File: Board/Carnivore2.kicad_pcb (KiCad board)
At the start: 2 copper layers, 99.1 x 64.3 mm, 153 parts, among them J1 Conn_01x02_Pin, T1 2SC945, T2 2SA733, T3 2SC945, T4 2SC945, T5 2SC945, T6 2SA733, U7 50 MHz, U8 DNI, X1 EDGE50/MSX, X2 HEADER_5X2, X3 HEADER_5X2

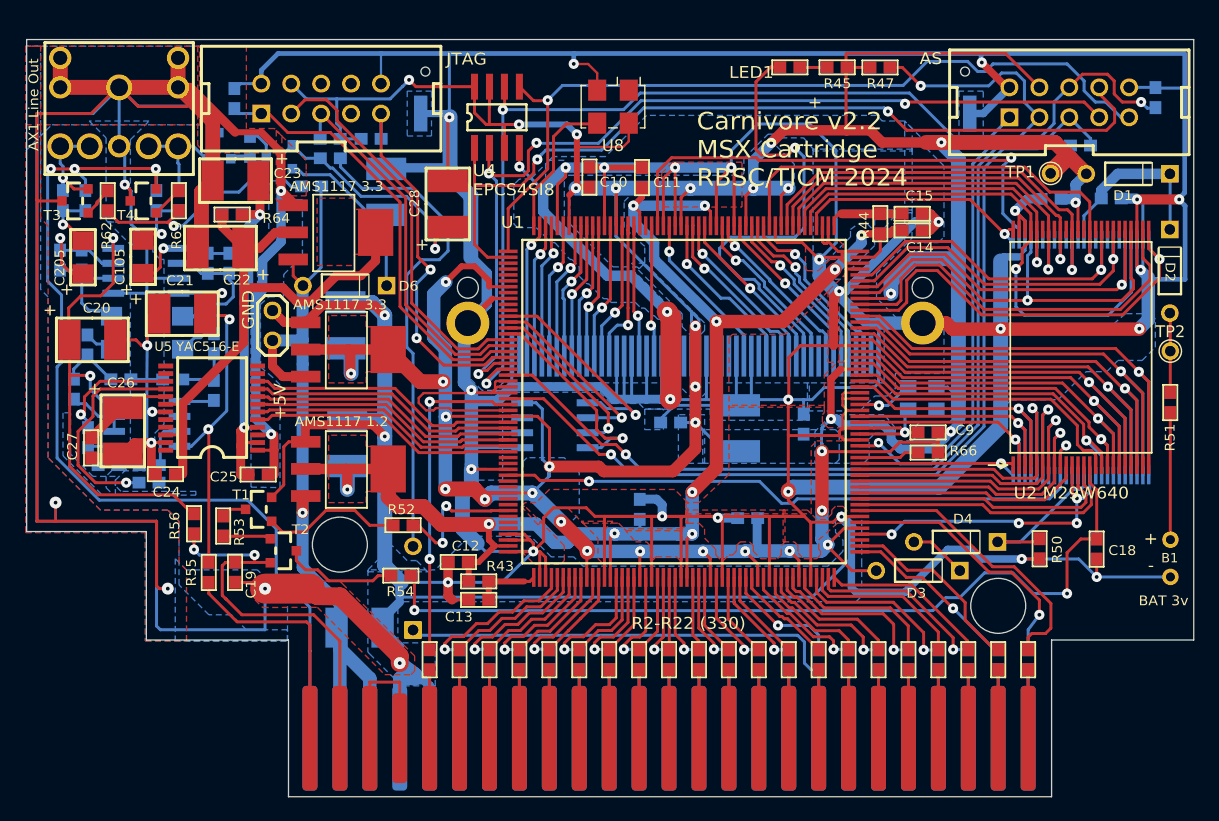
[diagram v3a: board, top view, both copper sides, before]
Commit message: Changed fpga from EP2C5 to EP2C8
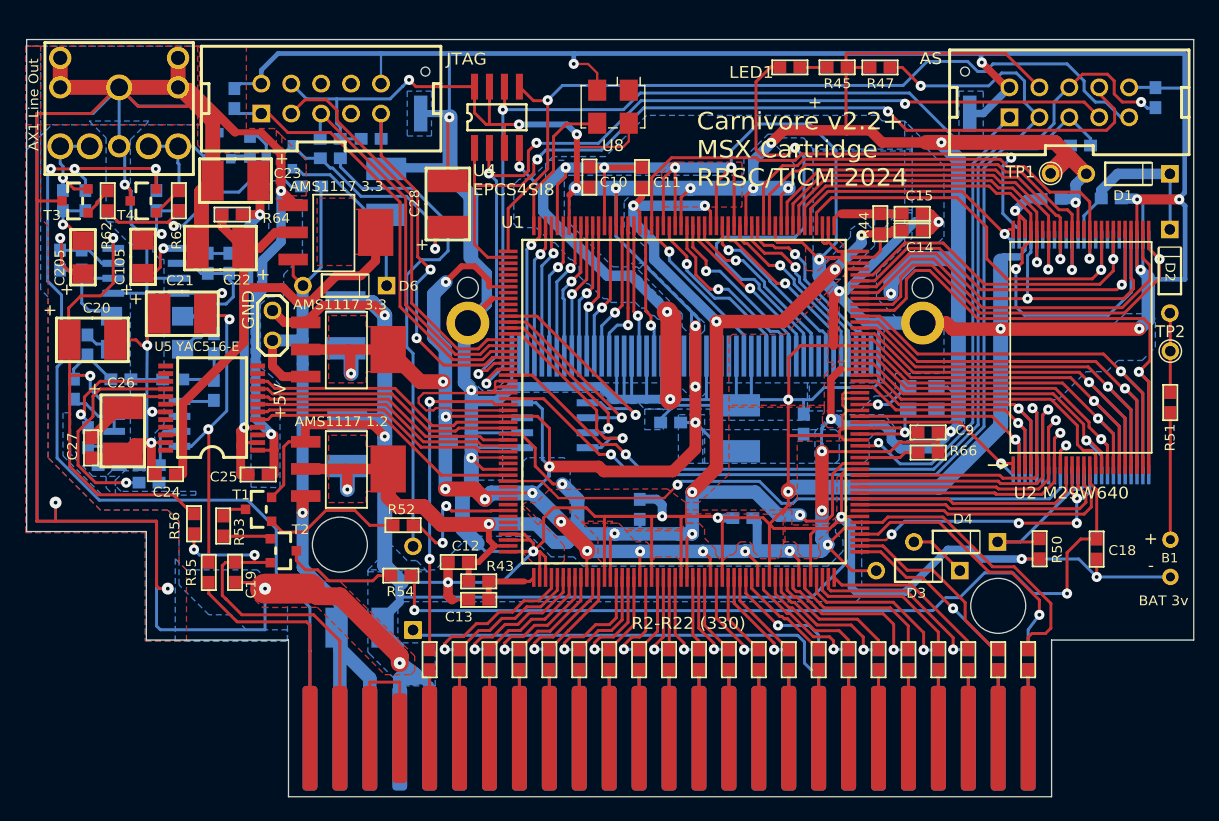
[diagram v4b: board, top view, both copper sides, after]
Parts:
- moved C8 0.41 mm to (155.4, 111.5)
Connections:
- U1 pad 107: unconnected-(U1B-IO,_LVDS41n_(INIT_DONE)-Pad107) -> /~{RWR}
- U1 pad 108: /~{RWR} -> /~{SLT_CS1}
- U1 pad 110: /~{SLT_CS1} -> /~{SLT_CS2}
- U1 pad 112: /~{SLT_CS2} -> /RA21
- U1 pad 113: /RA21 -> /~{RRP}
- U1 pad 114: /~{RRP} -> /RA20
- U1 pad 115: /RA20 -> /RA08
- U1 pad 116: /RA08 -> /RA09
- U1 pad 117: /RA09 -> /RA10
- U1 pad 118: /RA10 -> /RA11
- U1 pad 119: /RA11 -> /GND
- U1 pad 120: /RA15 -> /VCC1.2
- U1 pad 127: /RA14 -> /RA15
- U1 pad 128: /RA13 -> /RA14
- U1 pad 133: /RA12 -> /RA13
- U1 pad 134: /~{RRB} -> /RA12
- U1 pad 135: /RA18 -> /~{RRB}
- U1 pad 137: /RA17 -> /RA18
- U1 pad 138: /RA07 -> /RA17
- U1 pad 139: /RA06 -> /RA07
- U1 pad 141: /RA05 -> /RA06
- U1 pad 142: /RA04 -> /RA05
- U1 pad 143: /RA03 -> /RA04
- U1 pad 144: /RA02 -> /RA03
- U1 pad 145: /RA01 -> /RA02
- U1 pad 146: /RA00 -> /RA01
- U1 pad 147: /R~{E} -> /RA00
- U1 pad 149: /R~{G} -> /R~{E}
- U1 pad 150: /RDQ0 -> /R~{G}
- U1 pad 151: /RDQ1 -> /RDQ0
- U1 pad 152: /RDQ2 -> /RDQ1
- U1 pad 160: /RA16 -> /RDQ2
- U1 pad 161: /RDQ15A-1 -> /RA16
- U1 pad 162: /RDQ7 -> /RDQ15A-1
- U1 pad 163: /RDQ6 -> /RDQ7
- U1 pad 164: /RDQ5 -> /RDQ6
- U1 pad 165: /RDQ4 -> /RDQ5
- U1 pad 168: /RDQ3 -> /RDQ4
- U1 pad 169: /HD10 -> /RDQ3
- U1 pad 170: /HD09 -> /HD10
- U1 pad 171: /HD02 -> /HD09
- U1 pad 173: /HD08 -> /HD02
- U1 pad 175: /HD01 -> /HD08
- U1 pad 176: /HD00 -> /HD01
- U1 pad 179: /HA0 -> /HD00
- U1 pad 180: /~{HREG} -> /HA0
- U1 pad 181: /HA1 -> /~{HREG}
- U1 pad 182: /HA2 -> /HA1
- U1 pad 185: /~{HRST} -> /HA2
- U1 pad 187: /~{CSRAM} -> /~{HRST}
- U1 pad 188: /~{HWR} -> /~{CSRAM}
- U1 pad 189: unconnected-(U1A-IO,_LVDS19n,_DQ1T2/DQ1T11-Pad189) -> /~{HWR}
- U1 pad 32: /BICK -> /VCC1.2
- U1 pad 33: /CKS -> /BICK
- U1 pad 34: /MCLK -> /CKS
- U1 pad 35: /~{IC} -> /MCLK
- U1 pad 36: unconnected-(U1A-IO,_LVDS2n-Pad36) -> /GND
- U1 pad 39: /RA19 -> /~{IC}
- U1 pad 40: unconnected-(U1A-IO,_LVDS1p,_DQ1L8/_-Pad40) -> /RA19
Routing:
- net /VCC1.2: track 123.9 -> 155.3 mm, vias 10 -> 12
- net /RA01: track 43.1 -> 50.7 mm
- net /RDQ2: track 29.3 -> 36.5 mm
- net /GND: track 1229.9 -> 1233.3 mm
- net /RDQ4: track 35.9 -> 38.4 mm
- net /HD02: track 14.4 -> 16.0 mm
- net /RA15: track 14.5 -> 16.0 mm
- net /RA16: track 20.6 -> 21.9 mm
- net /RDQ15A-1: track 45.0 -> 46.2 mm
- net /RDQ7: track 28.9 -> 30.1 mm
- net /RDQ6: track 31.8 -> 33.1 mm
- net /RDQ5: track 31.9 -> 33.2 mm
- net /R~{E}: track 34.2 -> 33.0 mm
- net /HD00: track 14.5 -> 15.6 mm
- net /RA13: track 22.2 -> 23.2 mm
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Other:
- board text added: "Carnivore v2.2+ MSX Cartridge RBSC/TICM 2024"
- board text removed: "Carnivore v2.2 MSX Cartridge RBSC/TICM 2024"

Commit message: Changed audio DAC to modern type, added audio input, updated footprints
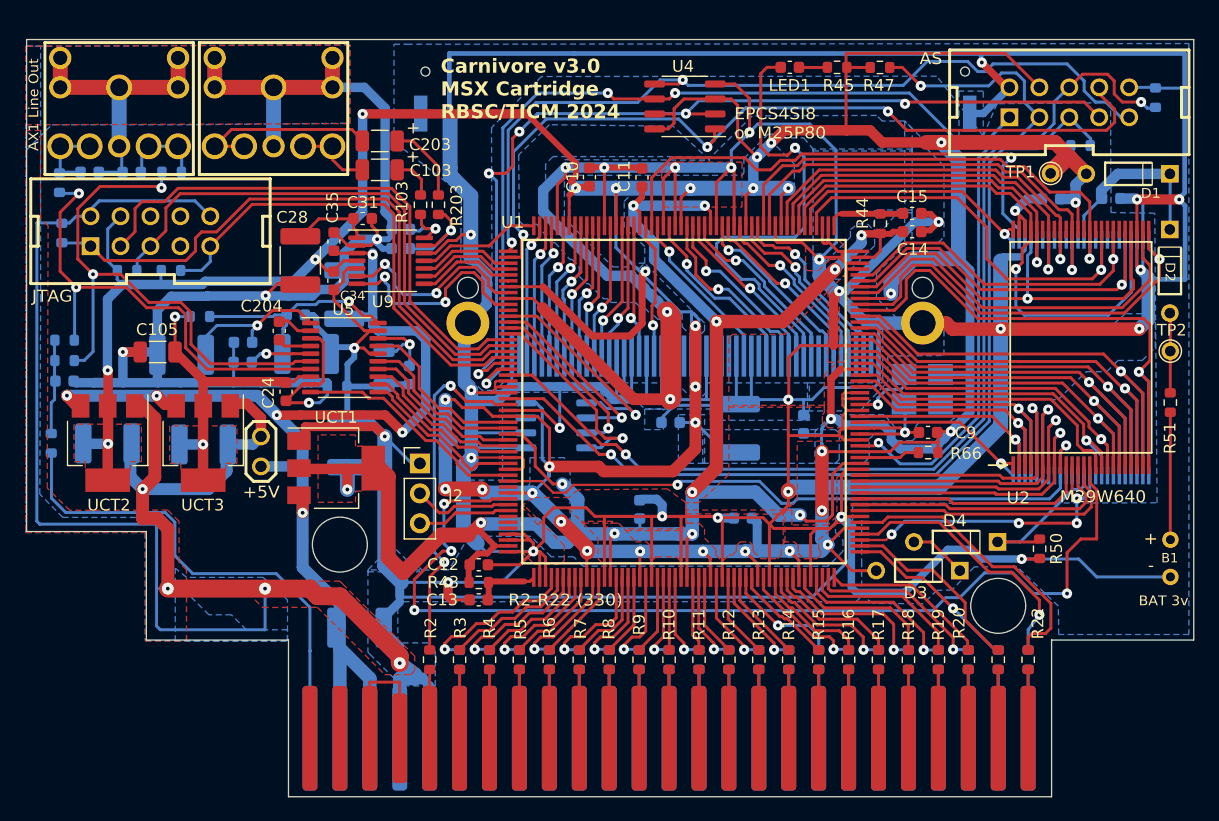
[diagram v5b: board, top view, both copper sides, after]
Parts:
- removed AU1, AU2: ~, Library:4558D_1
- removed C18, C19: 0.1mk, Library:C_0603_1
- removed C20, C21: 100mk 16v, Library:C_1812_1
- removed C202: 1n, Library:C_0603_1
- removed D5, D6: 1N4148, Library:DIODE_1N4148_1
- removed R101, R201, R52, R65: 10k, Library:R_0603_1
- removed R102, R202: 4.7k, Library:R_0603_1
- removed R105, R205: 1.8k, Library:R_0603_1
- removed R106, R206: 1k, Library:R_0603_1
- removed R53, R62, R63: 2.2k, Library:R_0603_1
- removed R54: 10, Library:R_0603_1
- removed R55, R56: 220, Library:R_0603_1
- removed T1, T3, T4, T5: 2SC945, Library:SOT-23(A1A2K)_1
- removed T2, T6: 2SA733, Library:SOT-23(A1A2K)_1
- removed U8: DNI, Oscillator:Oscillator_SMD_TXC_7C-4Pin_5.0x3.2mm_HandSoldering
- added AX2: {Value}, Library:ST-222_1, F.Cu at (115.5, 74.9)
- added C31: 100nF, Capacitor_SMD:C_0603_1608Metric, F.Cu at (123.1, 86.0)
- added C32: 100nF, Capacitor_SMD:C_0603_1608Metric, B.Cu at (126.3, 86.9)
- added C33: 100nF, Capacitor_SMD:C_0603_1608Metric, B.Cu at (126.3, 88.6)
- added C34: 100nF, Capacitor_SMD:C_0603_1608Metric, F.Cu at (120.7, 91.3)
- added C35: 100nF, Capacitor_SMD:C_0603_1608Metric, F.Cu at (120.7, 88.0)
- added C36: 2.2nF, Capacitor_SMD:C_0603_1608Metric, B.Cu at (97.8, 99.8)
- added J2: Conn_01x03_Pin, Connector_PinHeader_2.54mm:PinHeader_1x03_P2.54mm_Vertical, F.Cu at (128.0, 106.8)
- added R49: 470, Resistor_SMD:R_0603_1608Metric, B.Cu at (97.8, 98.1)
- added R99: 10, Resistor_SMD:R_0603_1608Metric, B.Cu at (120.9, 100.3)
- added U9: ~, Package_SO:TSSOP-14_4.4x5mm_P0.65mm, F.Cu at (125.5, 89.6)
- C1, C2, C3, C4: footprint Library:C_1812_1 -> Capacitor_SMD:C_1812_4532Metric
- C10, C11, C12, C13, C14, C15, C16, C17, C30, C5, C6, C7, C8, C9, LED1: footprint Library:C_0603_1 -> Capacitor_SMD:C_0603_1608Metric
- C101, C201: value 1n -> 2.2nF; footprint Library:C_0603_1 -> Capacitor_SMD:C_0603_1608Metric
- C102: value 1n -> 100nF; footprint Library:C_0603_1 -> Capacitor_SMD:C_0603_1608Metric
- C103, C203: value 4.7mk 25v -> 10uF 16V; footprint Library:C_1206_1 -> Capacitor_SMD:C_1206_3216Metric; moved to F.Cu
- C104: value 390p -> 2.2uF; footprint Library:C_0603_1 -> Capacitor_SMD:C_0603_1608Metric
- C105: value 4.7mk 25v -> 10uF 16V; footprint Library:C_1206_1 -> Capacitor_SMD:C_1206_3216Metric
- C204: value 390p -> 2.2uF; footprint Library:C_0603_1 -> Capacitor_SMD:C_0603_1608Metric; moved to F.Cu
- C205: value 4.7mk 25v -> 10uF 16V; footprint Library:C_1206_1 -> Capacitor_SMD:C_1206_3216Metric; moved to B.Cu
- C22: footprint Library:C_1812_1 -> Capacitor_SMD:C_1812_4532Metric; moved to B.Cu
- C23, C26: value 10mk -> 10uF 16V; footprint Library:C_1812_1 -> Capacitor_SMD:C_1812_4532Metric; moved to B.Cu
- C24: value 0.1mk -> 100nF; footprint Library:C_0603_1 -> Capacitor_SMD:C_0603_1608Metric
- C25, C27: value 0.1mk -> 100nF; footprint Library:C_0603_1 -> Capacitor_SMD:C_0603_1608Metric; moved to B.Cu
- C28: value 10mk -> 10uF 16v; footprint Library:C_1812_1 -> Capacitor_SMD:C_1812_4532Metric
- C29: value 22mk -> 10uF 16V; footprint Library:C_1812_1 -> Capacitor_SMD:C_1812_4532Metric
- R10, R11, R12, R13, R14, R15, R16, R17, R18, R19, R2, R20, R21, R22, R23, R24, R25, R26, R27, R28, R29, R3, R30, R31, R32, R33, R34, R35, R36, R37, R38, R39, R4, R40, R41, R42, R43, R44, R45, R46, R47, R48, R5, R50, R51, R57, R58, R59, R6, R66, R7, R8, R9: footprint Library:R_0603_1 -> Resistor_SMD:R_0603_1608Metric
- R103, R203: footprint Library:R_0603_1 -> Resistor_SMD:R_0603_1608Metric; moved to F.Cu
- R104, R204: value 100k -> 470; footprint Library:R_0603_1 -> Resistor_SMD:R_0603_1608Metric
- R60: value 10k -> 470; footprint Library:R_0603_1 -> Resistor_SMD:R_0603_1608Metric
- R61: value 2.2k -> 470; footprint Library:R_0603_1 -> Resistor_SMD:R_0603_1608Metric
- R64: footprint Library:R_0603_1 -> Resistor_SMD:R_0603_1608Metric; moved to B.Cu
- U4: footprint Library:EPCS4SI8_1 -> Package_SO:SO-8_3.9x4.9mm_P1.27mm
- U5: footprint Library:YAC516-E_1 -> Package_SO:TSSOP-20_4.4x6.5mm_P0.65mm
- U6: footprint Library:M93C46MN1_1 -> Package_SO:SO-8_3.9x4.9mm_P1.27mm
- U7: footprint Library:SG-310_1 -> Oscillator:Oscillator_SMD_SeikoEpson_SG8002CE-4Pin_3.2x2.5mm_HandSoldering
- UCT1, UCT2, UCT3: footprint Library:ADP3338_1 -> Package_TO_SOT_SMD:SOT-223
- moved R203 32.1 mm to (129.5, 84.8), turned to 90 degrees
- moved R61 30.3 mm to (96.7, 105.1), turned to -90 degrees
- moved C203 28.0 mm to (124.5, 79.4), turned to 180 degrees
- moved R60 27.3 mm to (97.8, 96.3)
- moved C205 27.2 mm to (124.9, 98.7)
- moved C201 24.9 mm to (99.9, 82.1), turned to 0 degrees
- moved C101 24.9 mm to (103.5, 82.1)
- moved C2 22.5 mm to (101.4, 105.1), turned to 180 degrees
- moved C103 21.7 mm to (124.5, 81.9), turned to 180 degrees
- moved UCT3 21.6 mm to (109.6, 105.1)
- moved R103 21.1 mm to (128.0, 84.8), turned to 90 degrees
- moved R58 20.5 mm to (103.1, 90.4)
- moved R59 20.3 mm to (106.8, 90.4), turned to 0 degrees
- moved C102 20.1 mm to (127.0, 99.3), turned to 90 degrees
- moved UCT2 19.7 mm to (101.5, 105.1)
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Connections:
- net /CONF_DONE renamed Net-(U1C-CONF_DONE)
- net /~{SLT_RESET_RAW} renamed Net-(R30-Pad2)
- AX1 pad 1: /GND -> /AGND
- AX1 pad 2: Net-(T5-E) -> Net-(AX1-Pad2)
- AX1 pad 3: Net-(T5-E) -> Net-(AX1-Pad2)
- AX1 pad 4: Net-(T3-E) -> Net-(AX1-Pad4)
- AX1 pad 5: Net-(T3-E) -> Net-(AX1-Pad4)
- AX1 pad M: /GND -> /AGND
- C101 pad 1: /GND -> /AGND
- C101 pad 2: Net-(AU1A-IN+) -> Net-(AX1-Pad4)
- C102 pad 1: Net-(C102-Pad1) -> /GND
- C102 pad 2: /GND -> Net-(C205-PLUS)
- C103 pad 2: Net-(AU2A-IN-) -> Net-(C103-MINUS)
- C104 pad 1: Net-(AU2A-IN-) -> Net-(U5-VNEG)
- C104 pad 2: Net-(AU2A-OUT) -> /AGND
- C105 pad 1: Net-(AU2A-OUT) -> /VCC3.3A
- C105 pad 2: Net-(C105-MINUS) -> /AGND
- C201 pad 1: /GND -> Net-(AX1-Pad2)
- C201 pad 2: Net-(AU1B-IN+) -> /AGND
- C203 pad 2: Net-(AU2B-IN-) -> Net-(C203-MINUS)
- C204 pad 1: Net-(AU2B-IN-) -> Net-(U5-CAPP)
- C204 pad 2: Net-(AU2B-OUT) -> Net-(U5-CAPM)
- C205 pad 1: Net-(AU2B-OUT) -> Net-(C205-PLUS)
- C205 pad 2: Net-(C205-MINUS) -> /GND
- C24 pad 1: /GND -> /AGND
- C26 pad 1: /GND -> /AGND
- C27 pad 1: /GND -> /AGND
- C28 pad 1: /GND -> /AGND
- C29 pad 1: /GND -> /AGND
- C29 pad 2: Net-(C29-PLUS) -> /VCC5
- R103 pad 1: Net-(C102-Pad1) -> Net-(U9-VinR)
- R104 pad 1: Net-(AU2A-IN-) -> Net-(U5-OUTL)
- R104 pad 2: Net-(AU2A-OUT) -> Net-(AX1-Pad4)
- R204 pad 1: Net-(AU2B-IN-) -> Net-(U5-OUTR)
- R204 pad 2: Net-(AU2B-OUT) -> Net-(AX1-Pad2)
- R60 pad 1: Net-(C28-PLUS) -> Net-(U5-OUTR)
- R60 pad 2: Net-(D5-A) -> Net-(C36-Pad1)
- R61 pad 1: Net-(T6-C) -> Net-(C36-Pad1)
- R61 pad 2: Net-(T3-B) -> /SLTSOUND
- U1 pad 10: unconnected-(U1A-IO,_LVDS7n,_DQ1L1/_-Pad10) -> /ADC_LRCK
- U1 pad 208: /KN0 -> /ADC_MD1
- U1 pad 3: unconnected-(U1A-IO,_LVDS9p_(CRC_ERROR)-Pad3) -> /ADC_MD0
- U1 pad 30: /LRCK -> /DAC_XSMT
- U1 pad 31: /SDATA -> /DAC_LRCK
- U1 pad 33: /BICK -> /DAC_DIN
- U1 pad 34: /CKS -> /DAC_BCK
- U1 pad 35: /MCLK -> /DAC_SCK
- U1 pad 37: unconnected-(U1A-IO,_VREFB1N1-Pad37) -> /DAC_FLT
- U1 pad 39: /~{IC} -> /DAC_DEMP
- U1 pad 4: unconnected-(U1A-IO,_LVDS9n_(CLKUSR)-Pad4) -> /ADC_DOUT
- U1 pad 43: unconnected-(U1A-IO-Pad43) -> /RVPPE
- U1 pad 44: unconnected-(U1A-IO,_LVDS0p-Pad44) -> Net-(J2-Pin_2)
- U1 pad 45: /RVPPE -> Net-(J2-Pin_3)
- U1 pad 5: unconnected-(U1A-IO,_LVDS8p-Pad5) -> /ADC_BCK
- U1 pad 8: unconnected-(U1A-IO,_LVDS7p,_DQ1L0/_-Pad8) -> /ADC_SCKI
- U2 pad 14: Net-(U2-Vpp/~{WP}) -> /RVPPE
- U5 pad 1: /GND -> Net-(C26-PLUS)
- U5 pad 10: /LRCK -> /DAC_DEMP
- U5 pad 11: unconnected-(U5-nc-Pad11) -> /DAC_FLT
- U5 pad 12: unconnected-(U5-nc-Pad12) -> /DAC_SCK
- U5 pad 13: unconnected-(U5-nc-Pad13) -> /DAC_BCK
- U5 pad 14: unconnected-(U5-nc-Pad14) -> /DAC_DIN
- U5 pad 15: Net-(U5-AOUTR) -> /DAC_LRCK
- U5 pad 16: Net-(U5-AOUTL) -> /GND
- U5 pad 17: Net-(C26-PLUS) -> /DAC_XSMT
- U5 pad 18: /VCC3.3A -> Net-(C205-PLUS)
- U5 pad 2: Net-(C23-PLUS) -> Net-(U5-CAPP)
- U5 pad 20: unconnected-(U5-nc-Pad20) -> Net-(C23-PLUS)
- U5 pad 3: /GND -> /AGND
- U5 pad 4: Net-(C23-PLUS) -> Net-(U5-CAPM)
- U5 pad 5: /~{IC} -> Net-(U5-VNEG)
- U5 pad 6: /MCLK -> Net-(U5-OUTL)
- U5 pad 7: /CKS -> Net-(U5-OUTR)
- U5 pad 8: /BICK -> /VCC3.3A
- U5 pad 9: /SDATA -> /AGND
- X1 pad 48: /VCC+12 -> unconnected-(X1-Pad48)
- X1 pad 50: /VCC-12 -> unconnected-(X1-Pad50)
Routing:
- net /GND: track 1233.3 -> 1036.6 mm, vias 43 -> 36
- net /AGND: track 0.00 -> 151.1 mm, vias 0 -> 4
- net /RVPPE: track 11.9 -> 87.1 mm, vias 2 -> 4
- net Net-(U2-Vpp/~{WP}): track 73.6 -> 0.00 mm, vias 2 -> 0
- net Net-(U5-OUTL): track 0.00 -> 47.1 mm, vias 0 -> 2
- net Net-(D5-A): track 41.8 -> 0.00 mm
- net /AV12+: track 40.5 -> 0.00 mm, vias 2 -> 0
- net Net-(U5-OUTR): track 0.00 -> 39.9 mm, vias 0 -> 2
- net /SLTSOUND: track 80.2 -> 42.4 mm, vias 3 -> 0
- net Net-(R30-Pad2): track 43.3 -> 6.14 mm
- net /VCC+12: track 33.7 -> 0.00 mm, vias 2 -> 0
- net /AV12-: track 33.5 -> 0.00 mm, vias 3 -> 0
- net /VCC5: track 72.5 -> 104.3 mm, vias 1 -> 6
- net /VCC3.3: track 430.3 -> 461.0 mm
- net /~{IC}: track 23.1 -> 0.00 mm
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- added copper zone on B.Cu, net /AGND
- added copper zone on F.Cu, net /AGND
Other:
- board text added: "AT93C46"
- board text added: "CY62167DV30"
- board text added: "Carnivore v3.0 MSX Cartridge RBSC/TICM 2024"
- board text added: "EPCS4SI8 or M25P80"
- board text added: "M29W640"
- board text added: "SG-310 50 MHz"
- board text removed: "AMS1117 1.2"
- board text removed: "AMS1117 3.3"
- board text removed: "AU1 4558D"
- board text removed: "AU2 4558D"
- board text removed: "C1"
- board text removed: "C10"
- board text removed: "C101"
- board text removed: "C102"
- board text removed: "C103"
- board text removed: "C104"
- board text removed: "C105"
- board text removed: "C11"
- board text removed: "C12"
- board text removed: "C13"
- board text removed: "C14"
- board text removed: "C15"
- board text removed: "C16"
- board text removed: "C17"
- board text removed: "C18"
- board text removed: "C19"
- board text removed: "C2"
- board text removed: "C20"
- board text removed: "C201"
- board text removed: "C202"
- board text removed: "C203"
- board text removed: "C204"
- board text removed: "C205"
- board text removed: "C21"
- board text removed: "C22"
- board text removed: "C23"
- board text removed: "C24"
- board text removed: "C25"
- board text removed: "C26"
- board text removed: "C27"
- board text removed: "C28"
- board text removed: "C29"
- board text removed: "C3"
- board text removed: "C4"
- board text removed: "C5"
- board text removed: "C6"
- board text removed: "C7"
- board text removed: "C8"
- board text removed: "C9"
- board text removed: "Carnivore v2.2+ MSX Cartridge RBSC/TICM 2024"
- board text removed: "D3"
- board text removed: "D4"
- board text removed: "D5"
- board text removed: "D6"
- board text removed: "GND"
- board text removed: "LED1"
- board text removed: "R101"
- board text removed: "R102"
- board text removed: "R103"
- board text removed: "R104"
- board text removed: "R105"
- board text removed: "R106"
- board text removed: "R201"
- board text removed: "R202"
- board text removed: "R203"
- board text removed: "R204"
- board text removed: "R205"
- board text removed: "R206"
- board text removed: "R43"
- board text removed: "R44"
- board text removed: "R45"
- board text removed: "R46"
- board text removed: "R47"
- board text removed: "R48"
- board text removed: "R50"
- board text removed: "R51"
- board text removed: "R52"
- board text removed: "R53"
- board text removed: "R54"
- board text removed: "R55"
- board text removed: "R56"
- board text removed: "R57"
- board text removed: "R58"
- board text removed: "R61"
- board text removed: "R62"
- board text removed: "R63"
- board text removed: "R64"
- board text removed: "R65"
- board text removed: "R66"
- board text removed: "T1"
- board text removed: "T2"
- board text removed: "T3"
- board text removed: "T4"
- board text removed: "T5"
- board text removed: "T6"
- board text removed: "U2 M29W640"
- board text removed: "U3 CY62167DV30"
- board text removed: "U4 EPCS4SI8"
- board text removed: "U5 YAC516-E"
- board text removed: "U6 AT93C46"
- board text removed: "XCG1 SG-310 50 MHz"

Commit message: Updated more footprints 3D view complete
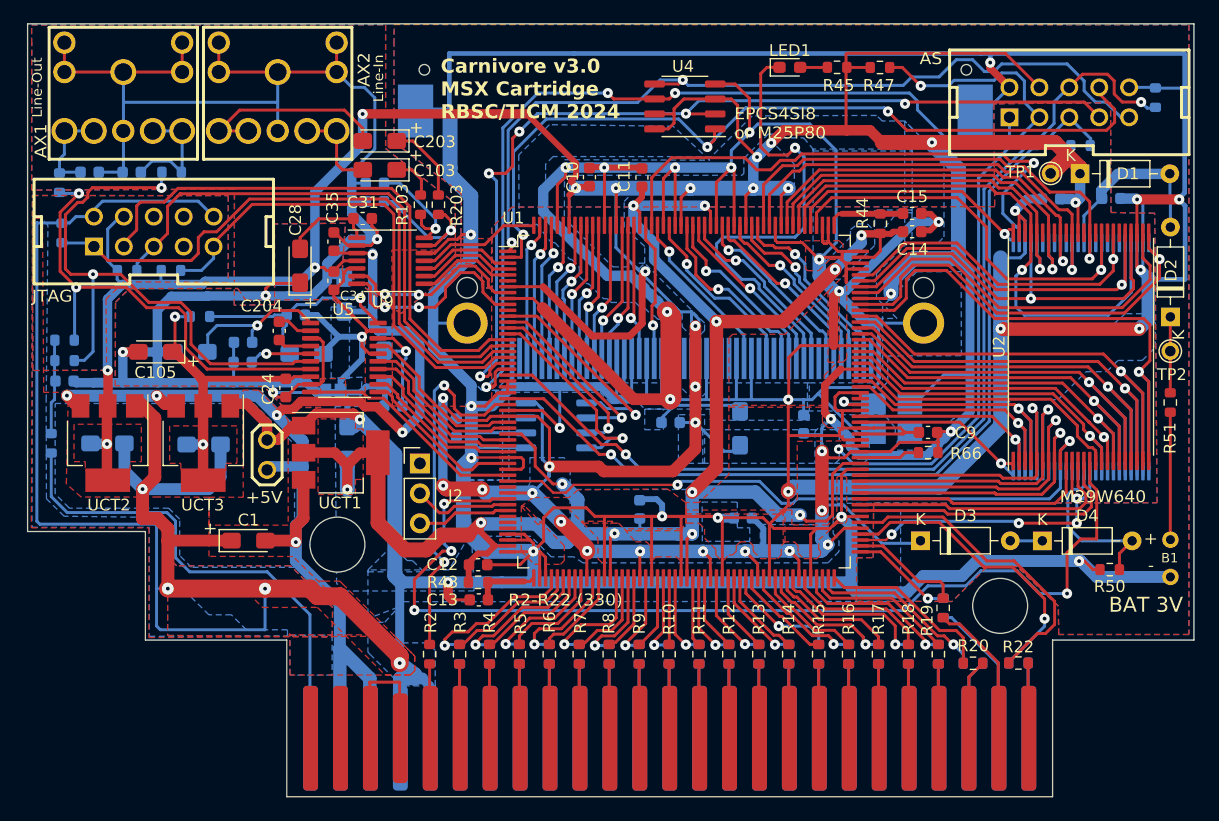
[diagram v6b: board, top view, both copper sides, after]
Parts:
- AX1, AX2: value {Value} -> SJ1-3523N
- B1: value BAT -> BAT 3V
- C1: value 10mk -> 10uF 16V; footprint Capacitor_SMD:C_1812_4532Metric -> Capacitor_Tantalum_SMD:CP_EIA-3216-10_Kemet-I_Pad1.58x1.35mm_HandSolder; moved to F.Cu
- C10, C11, C12, C13, C14, C15, C16, C17, C30, C5, C6, C7, C8, C9: value 0.1mk -> 100nF
- C103, C105, C203, C205: footprint Capacitor_SMD:C_1206_3216Metric -> Capacitor_Tantalum_SMD:CP_EIA-3216-10_Kemet-I_Pad1.58x1.35mm_HandSolder
- C2, C22, C3, C4: value 10mk -> 10uF 16V; footprint Capacitor_SMD:C_1812_4532Metric -> Capacitor_Tantalum_SMD:CP_EIA-3216-10_Kemet-I_Pad1.58x1.35mm_HandSolder
- C23, C26, C29: footprint Capacitor_SMD:C_1812_4532Metric -> Capacitor_Tantalum_SMD:CP_EIA-3216-10_Kemet-I_Pad1.58x1.35mm_HandSolder
- C28: value 10uF 16v -> 10uF 16V; footprint Capacitor_SMD:C_1812_4532Metric -> Capacitor_Tantalum_SMD:CP_EIA-3216-10_Kemet-I_Pad1.58x1.35mm_HandSolder
- D1, D2: value D9 -> 1N4148; footprint Library:DIODE_1N4148_1 -> Diode_THT:D_DO-35_SOD27_P7.62mm_Horizontal
- D3, D4: footprint Library:DIODE_1N4148_1 -> Diode_THT:D_DO-35_SOD27_P7.62mm_Horizontal
- LED1: value ~ -> 150060YS75000; footprint Capacitor_SMD:C_0603_1608Metric -> LED_SMD:LED_0603_1608Metric_Pad1.05x0.95mm_HandSolder
- R10, R11, R12, R13, R14, R15, R16, R17, R18, R19, R2, R20, R21, R22, R23, R24, R25, R26, R27, R28, R29, R3, R30, R31, R32, R33, R34, R35, R36, R37, R38, R39, R4, R40, R41, R42, R5, R6, R7, R8, R9: value 331 -> 330E
- R104, R204, R49, R60, R61: value 470 -> 470E
- R43, R44, R64: value 10 -> 10E
- R45: value 220 -> 220E
- R57: value 1K -> 1k
- R99: value 10 -> 0E; footprint Resistor_SMD:R_0603_1608Metric -> Jumper:SolderJumper-2_P1.3mm_Bridged_Pad1.0x1.5mm
- U1: value ~ -> EP2C8Q208C8N; footprint Library:EP2C5Q208C8_1 -> Package_QFP:PQFP-208_28x28mm_P0.5mm
- U2: value ~ -> MX29LV640ETTI-70G; footprint Library:M29W320DXXXNXX_1 -> Package_SO:TSOP-I-48_18.4x12mm_P0.5mm
- U3: value ~ -> RMLV1616AGSA-5S#KA0; footprint Library:CY62167DV30_1 -> Package_SO:TSOP-I-48_18.4x12mm_P0.5mm
- U4: value ~ -> M25P80-VMN3TPB
- U5: value ~ -> PCM5101APWR
- U6: value ~ -> AT93C46DN-SH-T
- U7: value 50 MHz -> SG3225CAN 50.0000M-TJGA6; footprint Oscillator:Oscillator_SMD_SeikoEpson_SG8002CE-4Pin_3.2x2.5mm_HandSoldering -> Library:SG3225CAN
- U9: value ~ -> PCM1808PWR
- UCT1: value 1.2v -> AP2114HA-1.2TRG1
- UCT2, UCT3: value 3.3v -> AP2111H-3.3TRG1
- X2, X3: value HEADER_5X2 -> 302-S101
- XC1: value ~ -> 101D-TAAB-R01; footprint Library:CF-50-001_1 -> Library:CF-Card_101D-TAAB-R01
- moved XC1 23.4 mm to (151.3, 94.8), turned to 90 degrees
- moved C1 12.0 mm to (113.4, 113.4), turned to 0 degrees
- moved U3 11.6 mm to (184.1, 97.8), turned to 90 degrees
- moved U2 11.6 mm to (184.1, 96.9)
- moved D4 7.35 mm to (180.8, 113.4)
- moved R21 6.42 mm to (172.4, 119.1)
- moved R24 6.40 mm to (172.4, 119.1)
- moved R50 6.21 mm to (186.5, 115.8), turned to 180 degrees
- moved C33 4.55 mm to (124.1, 84.6)
- moved C32 4.50 mm to (124.1, 83.0)
- moved D1 4.08 mm to (184.0, 82.2)
- moved D2 3.87 mm to (191.7, 94.4)
- moved U7 3.61 mm to (168.0, 103.0)
- moved C102 2.95 mm to (125.7, 101.9), turned to 0 degrees
- moved D3 2.55 mm to (170.4, 113.4)
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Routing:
- net /GND: track 1036.6 -> 1017.3 mm, vias 36 -> 35
- net /AGND: track 151.1 -> 168.7 mm
- net /VCC3.3: track 461.0 -> 472.6 mm
- net /~{SLT_SLTSEL}: track 16.5 -> 9.59 mm
- net Net-(R21-Pad1): track 5.82 -> 12.7 mm
- net Net-(R24-Pad2): track 5.82 -> 12.6 mm
- net /~{SLT_CS12}: track 15.2 -> 8.74 mm
- net /VCC5: track 104.3 -> 109.5 mm
- net Net-(U9-VinR): track 5.73 -> 9.92 mm
- net /DCLK: track 72.5 -> 75.9 mm
- net Net-(U9-VinL): track 9.01 -> 12.1 mm
- net Net-(AX1-Pad4): track 7.31 -> 10.3 mm
- net /~{SLT_CS1}: track 22.9 -> 25.5 mm
- net Net-(U5-OUTL): track 47.1 -> 49.5 mm
- net /~{CSRAM}: track 44.4 -> 46.8 mm
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- added copper zone on B.Cu, net /VCC1.2
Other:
- board size 99.1 x 64.3 mm -> 99 x 65.6 mm
- board text added: "Line-In"
- board text added: "Line-Out"
- board text removed: "AX1 Line Out"
- board text removed: "BAT 3v"
- board text removed: "D1"
- board text removed: "D2"
- board text removed: "U1"
